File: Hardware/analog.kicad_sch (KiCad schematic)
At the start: 27 parts, among them J1 Screw_Terminal_01x04, J2 Screw_Terminal_01x03, J3 Screw_Terminal_01x03, J4 Screw_Terminal_01x03, U1 THVD1400D

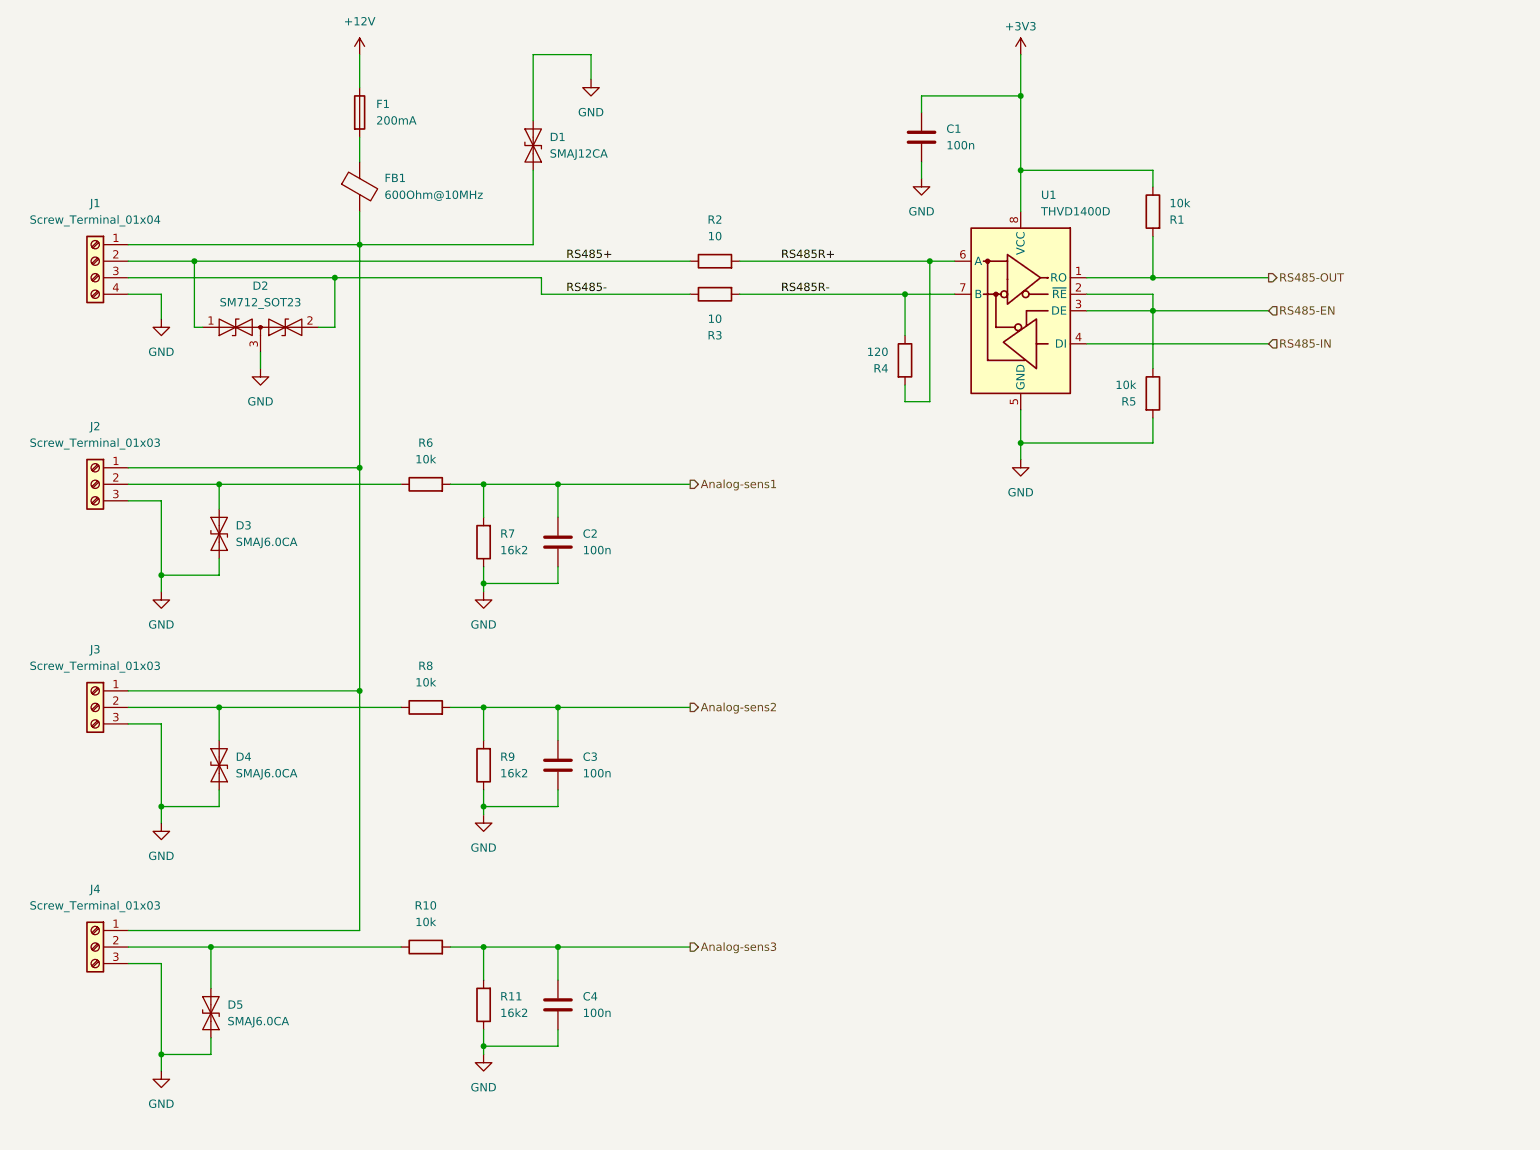
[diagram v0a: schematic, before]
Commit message: changed LP anti-aliasing filter to 2nd order RC
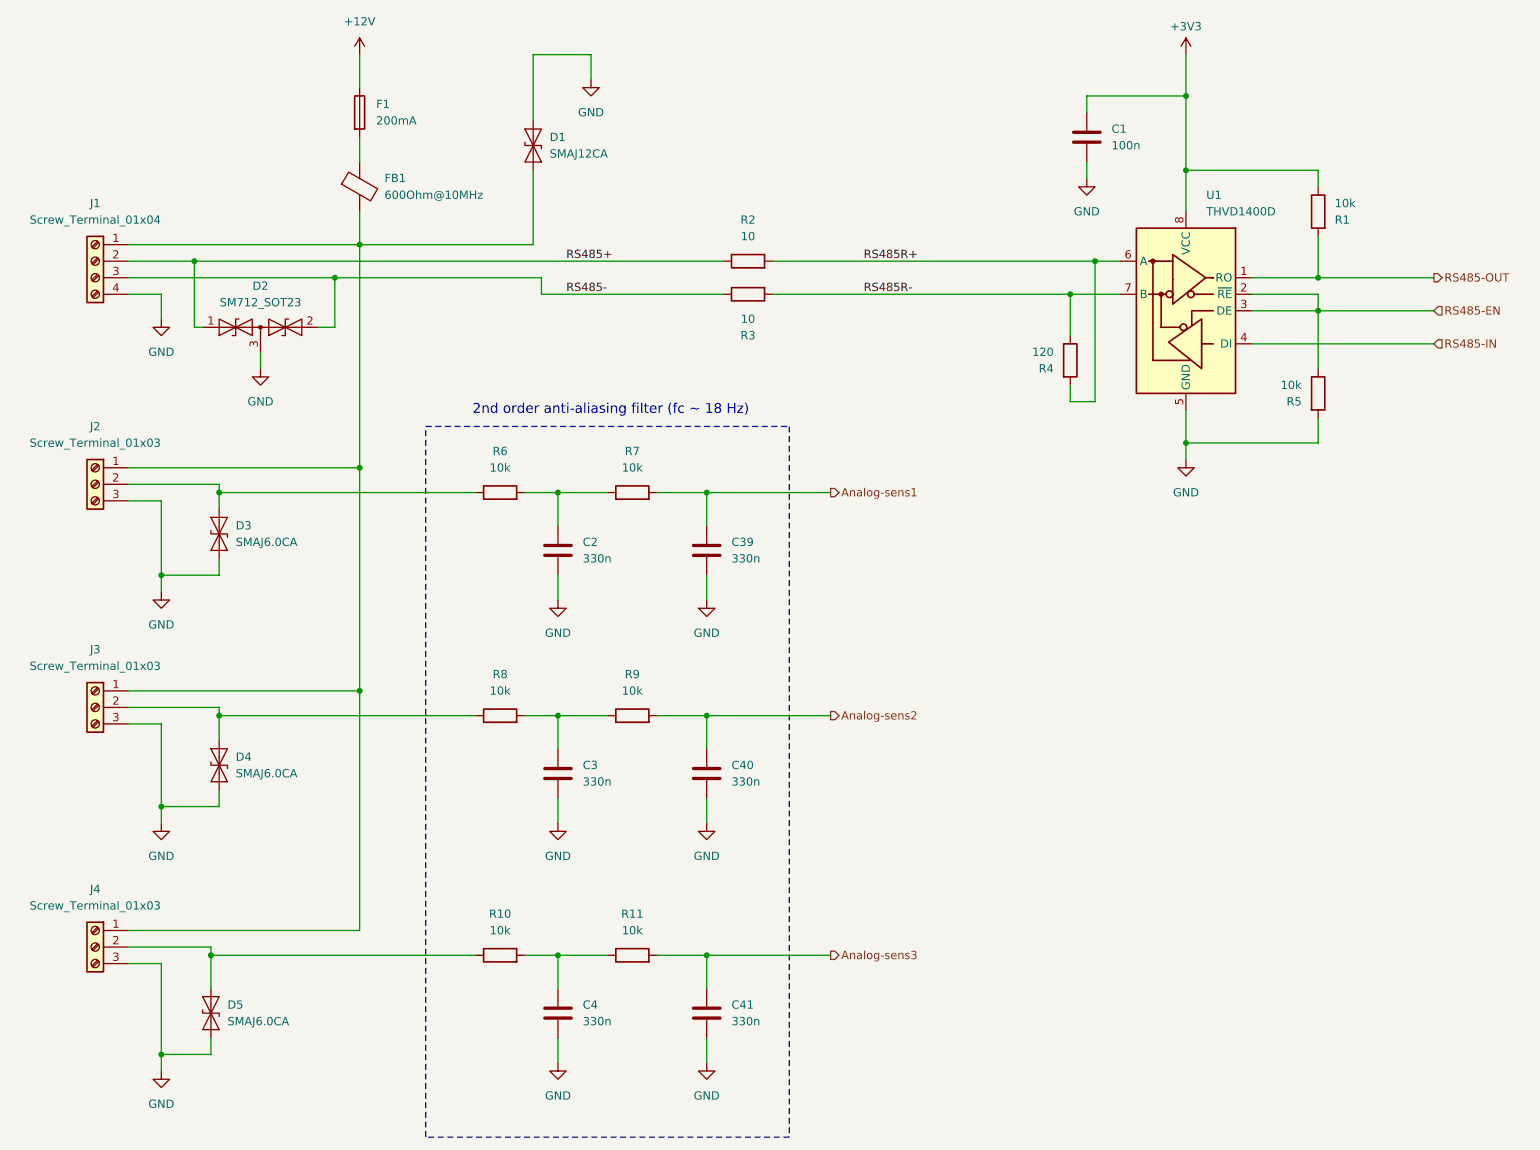
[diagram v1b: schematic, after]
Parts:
- added C39, C40, C41: 330n, Capacitor_SMD:C_0603_1608Metric, symbol Device:C
- C2, C3, C4: value 100n -> 330n
- R11, R7, R9: value 16k2 -> 10k
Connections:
- net Analog-sens1: now also C39.1; no longer C2.1, R6.2
- net Analog-sens2: now also C40.1; no longer C3.1, R8.2
- net Analog-sens3: now also C41.1; no longer C4.1, R10.2
- net GND: now also C39.2, C40.2, C41.2; no longer R11.1, R7.1, R9.1
- new net: C4.1, R10.2, R11.1
- new net: C2.1, R6.2, R7.1
- new net: C3.1, R8.2, R9.1
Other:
- note added: "2nd order anti-aliasing filter (fc ~ 18 Hz)"
- moved on the sheet: C1, C2, R1, R2, R3, R4, R5, R6, U1
